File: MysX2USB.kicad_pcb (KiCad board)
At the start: 2 copper layers, 15.9 x 17.6 mm, 9 parts, among them P1 USB, P2 MYSX_1.2, P3 supply, U1 FT230XS

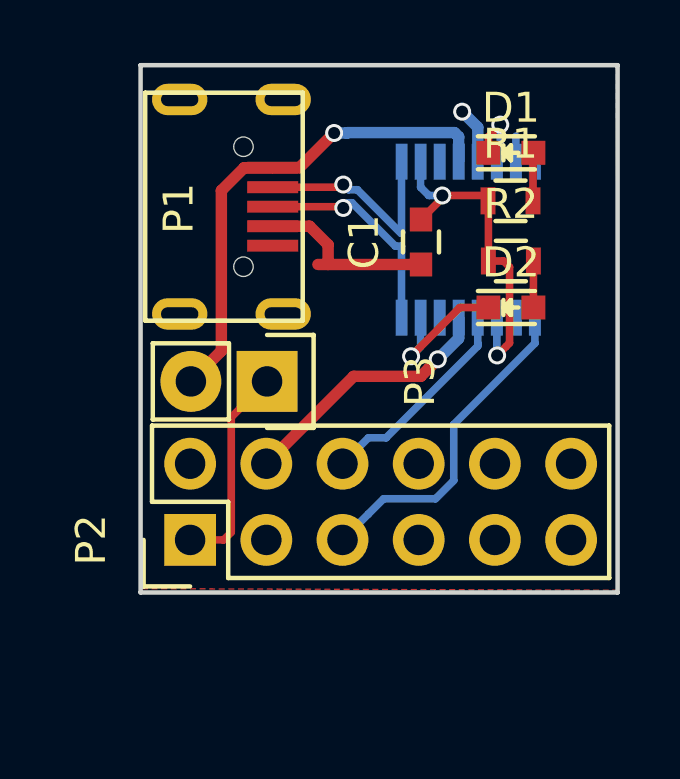
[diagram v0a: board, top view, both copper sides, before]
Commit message: Changed to use MysX1.1, and made the pcb smaller. Added pdf of schematics
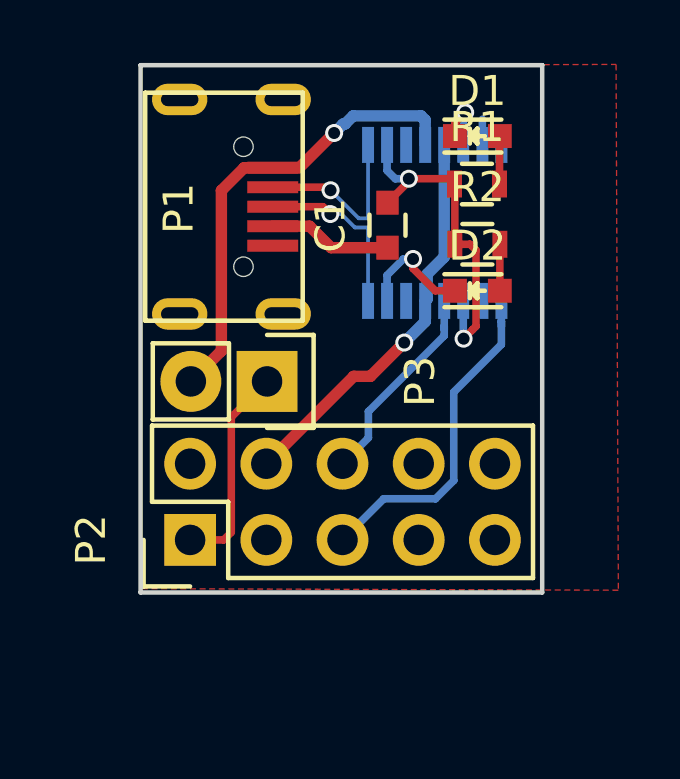
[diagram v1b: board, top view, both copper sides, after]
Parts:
- P2: footprint mysensors_connectors:MYSX_1.2 -> mysensors_connectors:MYSX_1.1
- moved D1 1.25 mm to (125.7, 111.9)
- moved D2 1.25 mm to (125.7, 117.1)
- moved R2 1.25 mm to (125.7, 115.5)
- moved C1 1.25 mm to (122.7, 114.9)
- moved R1 1.25 mm to (125.7, 113.5)
- moved U1 1.25 mm to (124.3, 114.8)
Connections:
- P2 pad 10: Net-(P2-Pad10) -> (no net)
- P2 pad 9: Net-(P2-Pad9) -> (no net)
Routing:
- net /D+: track 7.37 -> 5.91 mm
- net +5V: track 16.4 -> 15.5 mm
- net /D-: track 7.39 -> 6.59 mm
- net Net-(D2-Pad1): track 4.67 -> 3.97 mm
- net GND: track 16.9 -> 17.5 mm, vias 2 -> 1
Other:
- board size 15.9 x 17.6 mm -> 13.4 x 17.6 mm

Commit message: Updated to MysX2.0
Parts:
- added D3: TRGT, LEDs:LED-0603, F.Cu at (123.2, 115.3)
- added R3: R, Resistors_SMD:R_0603_HandSoldering, F.Cu at (123.2, 118.8)
- D1: value LED -> RX
- D2: value LED -> TX
- P1: value USB -> USB_A
- P2: value MYSX_1.2 -> MYSX_2.0; footprint mysensors_connectors:MYSX_1.1 -> mysensors_connectors:MYSX_2.0_SOCKET
- R1, R2: footprint Resistors_SMD:R_0603 -> Resistors_SMD:R_0603_HandSoldering
- U1: value FT230XS -> FT231XS; footprint Housings_SSOP:SSOP-16_3.9x4.9mm_Pitch0.635mm -> Housings_SSOP:SSOP-20_4.4x6.5mm_Pitch0.65mm
- moved P3 5.86 mm to (115.7, 125.2), turned to 180 degrees
- moved R1 5.26 mm to (125.1, 118.8), turned to 90 degrees
- moved P2 3.49 mm to (119.6, 125.2)
- moved R2 3.46 mm to (126.9, 118.8), turned to 90 degrees
- moved D1 3.44 mm to (125.1, 115.3), turned to 270 degrees
- moved D2 2.18 mm to (126.9, 115.3), turned to 270 degrees
- moved P1 1.40 mm to (114.1, 115.6)
- moved C1 0.97 mm to (121.7, 114.7), turned to 270 degrees
- moved U1 0.72 mm to (124.9, 115.2), turned to 180 degrees
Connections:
- P2 pad 7: Net-(P2-Pad7) -> /RST
- U1 pad 1: /TXD -> /RST
- U1 pad 10: Net-(C1-Pad2) -> Net-(D2-Pad1)
- U1 pad 11: Net-(U1-Pad11) -> /D+
- U1 pad 12: +5V -> /D-
- U1 pad 13: GND -> Net-(C1-Pad2)
- U1 pad 14: Net-(D1-Pad1) -> Net-(U1-Pad14)
- U1 pad 15: Net-(U1-Pad15) -> +5V
- U1 pad 16: Net-(U1-Pad16) -> GND
- U1 pad 5: GND -> Net-(U1-Pad5)
- U1 pad 6: Net-(U1-Pad6) -> GND
- U1 pad 7: Net-(D2-Pad1) -> Net-(U1-Pad7)
- U1 pad 8: /D+ -> Net-(U1-Pad8)
- U1 pad 9: /D- -> Net-(U1-Pad9)
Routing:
- net /RST: track 0.00 -> 17.8 mm
- net GND: track 17.5 -> 3.63 mm, vias 1 -> 2
- net /TXD: track 11.4 -> 19.4 mm
- net Net-(P2-Pad3): track 0.00 -> 5.84 mm
- net Net-(C1-Pad2): track 11.6 -> 16.0 mm
- net /RXD: track 6.93 -> 10.1 mm
- net Net-(P2-Pad1): track 7.00 -> 3.84 mm
- net Net-(D2-Pad1): track 3.97 -> 6.07 mm
- net Net-(D1-Pad1): track 2.25 -> 3.96 mm
- net Net-(D3-Pad2): track 0.00 -> 1.58 mm
- net Net-(U1-Pad15): track 0.85 -> 0.00 mm
- net /D-: track 6.59 -> 5.76 mm
- net +5V: track 15.5 -> 14.7 mm
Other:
- board size 13.4 x 17.6 mm -> 15 x 17 mm

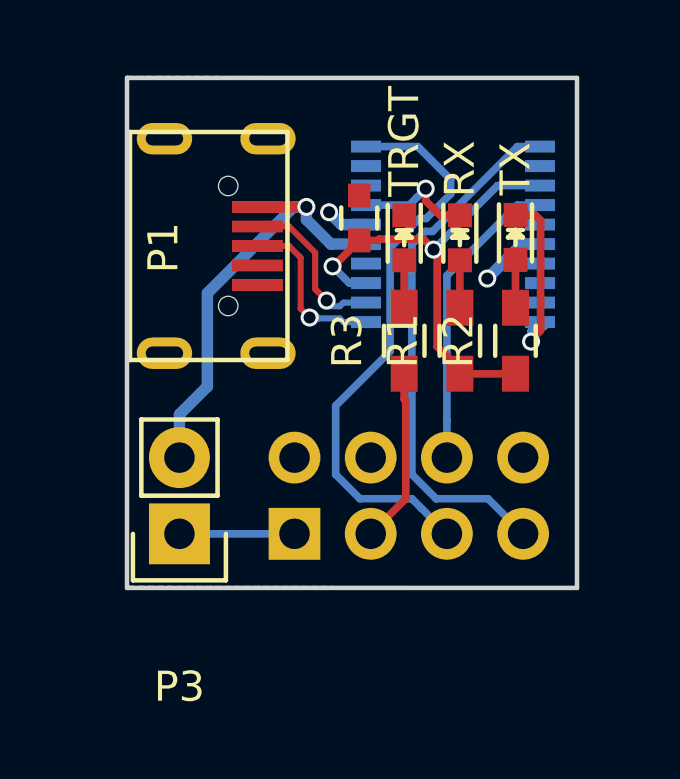
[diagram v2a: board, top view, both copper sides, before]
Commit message: Added copper pour to bottom layer
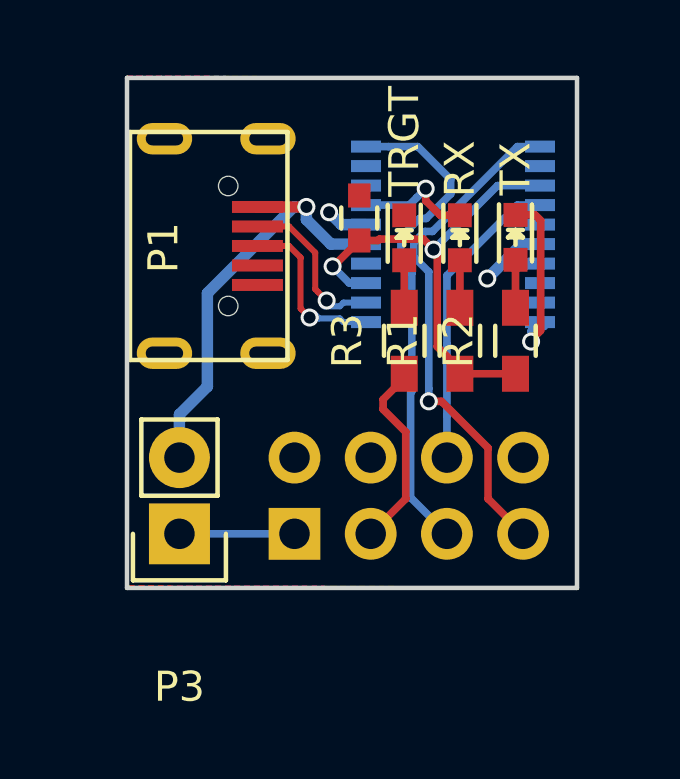
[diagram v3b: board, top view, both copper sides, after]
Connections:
- P1 pad 6: (no net) -> GND
- P1 pad 7: (no net) -> GND
- P1 pad 8: (no net) -> GND
- P1 pad 9: (no net) -> GND
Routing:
- net /TXD: track 19.4 -> 16.6 mm
- net /RST: track 17.8 -> 17.0 mm, vias 0 -> 1
- net Net-(P2-Pad3): track 5.84 -> 6.42 mm
- added copper zone on B.Cu, net GND
